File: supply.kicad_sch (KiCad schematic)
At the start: 62 parts, among them Q1 BSS138PW,115, Q6 BSS138PW,115, U21 TPS62A06DRLR, U22 TPS62A06DRLR, U40 SIC431AED-T1-GE3

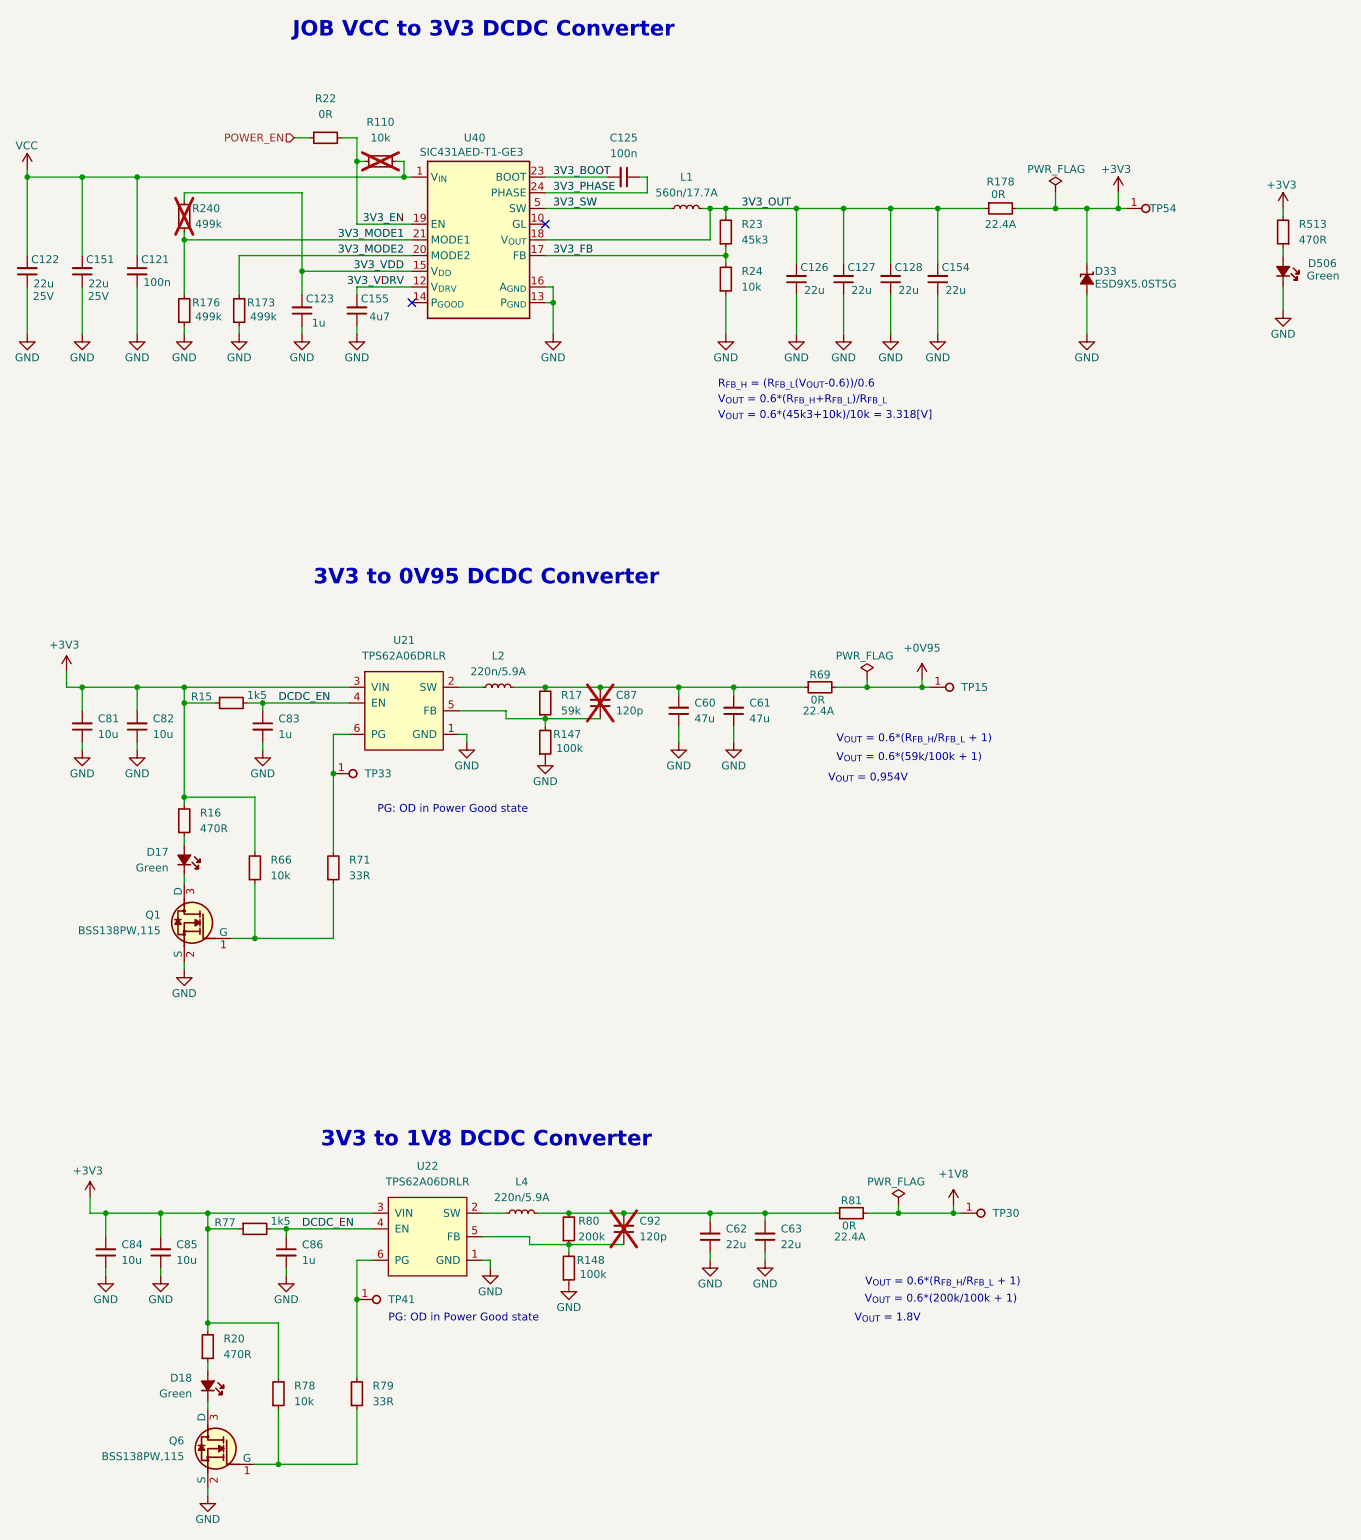
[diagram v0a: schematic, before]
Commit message: [#100765] Reset designators
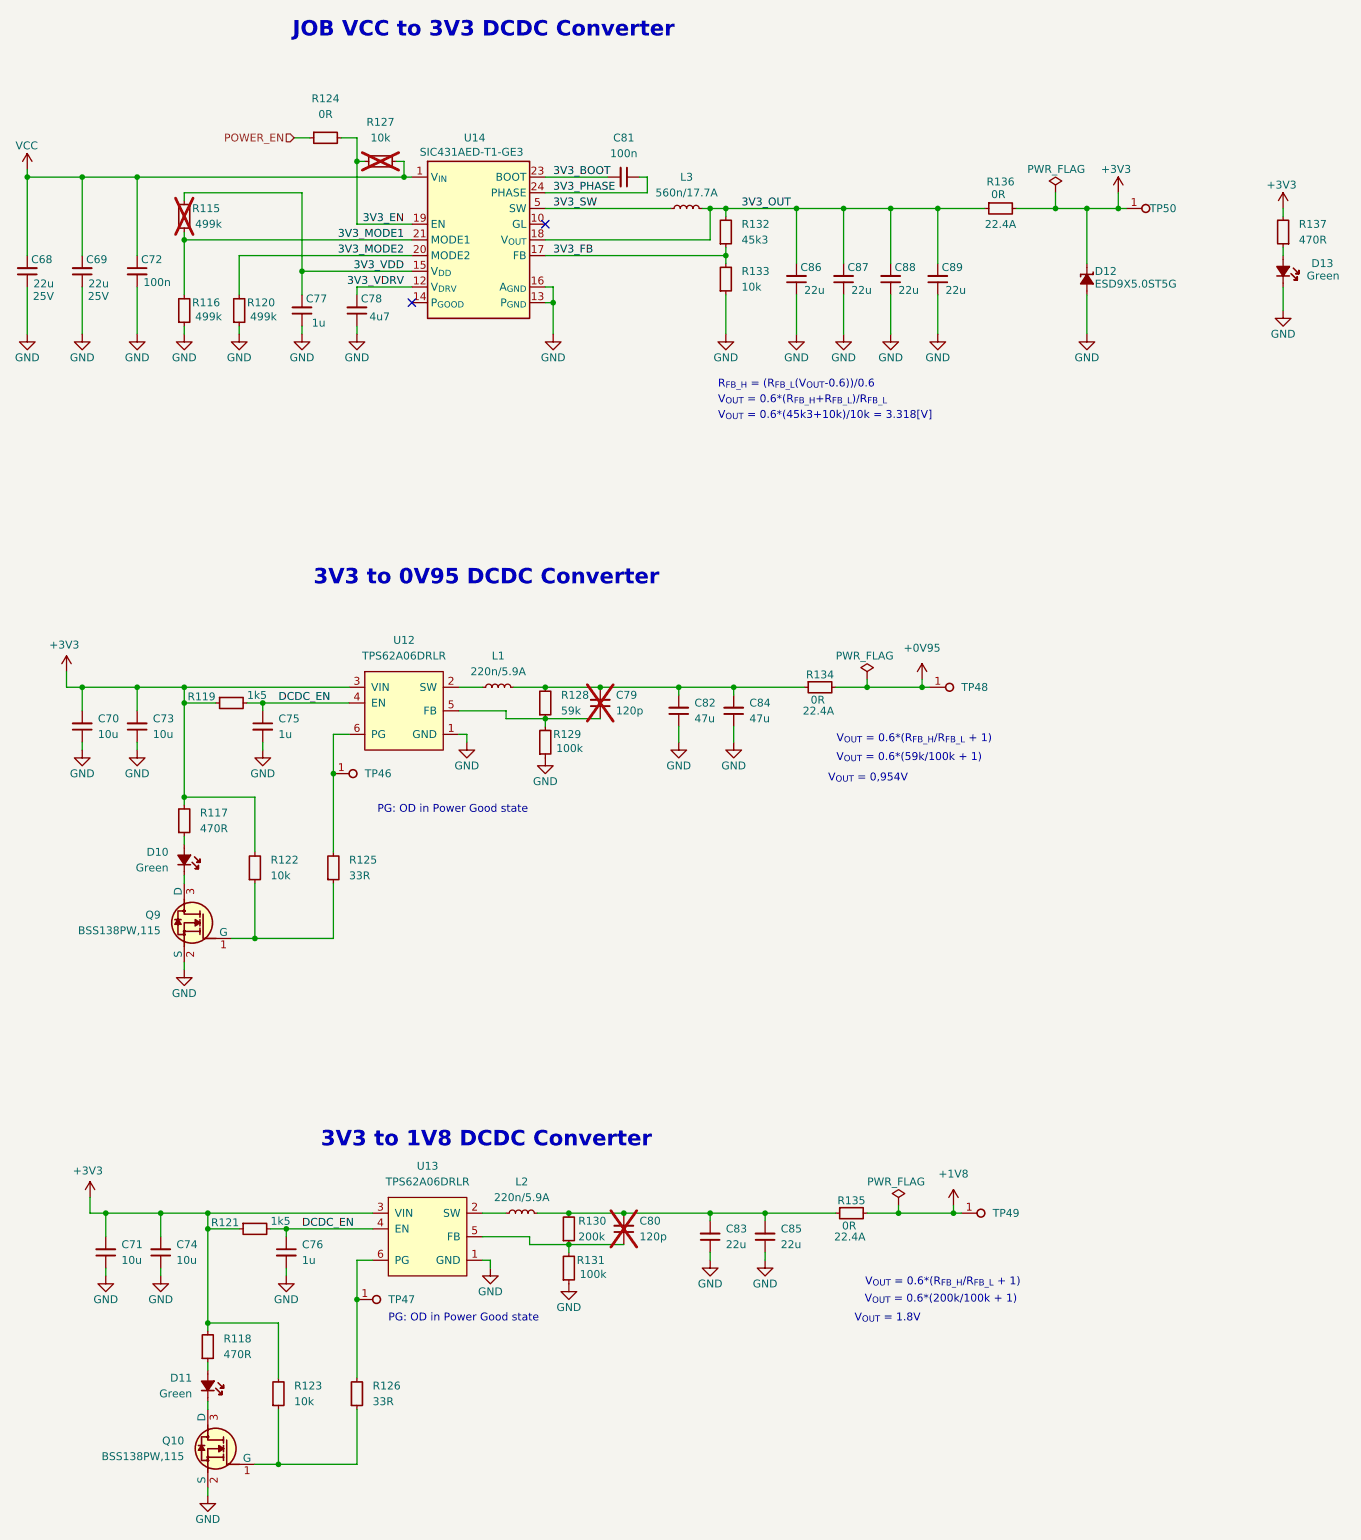
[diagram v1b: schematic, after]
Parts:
- renumbered C122 to C68, C151 to C69, C81 to C70, C84 to C71, C121 to C72, C82 to C73, C85 to C74, C83 to C75, C86 to C76, C123 to C77, C155 to C78, C87 to C79, C92 to C80, C125 to C81, C60 to C82, C62 to C83, C61 to C84, C63 to C85, C126 to C86, C127 to C87, C128 to C88, C154 to C89, D17 to D10, D18 to D11, D33 to D12, D506 to D13, L2 to L1, L4 to L2, L1 to L3, Q6 to Q10, Q1 to Q9, R240 to R115, R176 to R116, R16 to R117, R20 to R118, R15 to R119, R173 to R120, R77 to R121, R66 to R122, R78 to R123, R22 to R124, R71 to R125, R79 to R126, R110 to R127, R17 to R128, R147 to R129, R80 to R130, R148 to R131, R23 to R132, R24 to R133, R69 to R134, R81 to R135, R178 to R136, R513 to R137, TP33 to TP46, TP41 to TP47, TP15 to TP48, TP30 to TP49, TP54 to TP50, U21 to U12, U22 to U13, U40 to U14

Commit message: [#100765] Prettify schematic
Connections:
- net DCDC_EN: no longer names the net of C76.1, R121.2, U13.4 (EN)
- net DCDC_EN: no longer C75.1, R119.2, U12.4 (EN)
- new net: C75.1, R119.2, U12.4 (EN)
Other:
- note removed: "PG: OD in Power Good state"
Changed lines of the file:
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@@
 		)
 	)
-	(text "PG: OD in Power Good state"
-		(exclude_from_sim no)
-		(at 185.674 156.972 0)
-		(effects
-			(font
-				(size 1.27 1.27)
-			)
-		)
-	)
 	(text "3V3 to 0V95 DCDC Converter"
 		(exclude_from_sim no)
@@
 		)
 	)
-	(text "PG: OD in Power Good state"
-		(exclude_from_sim no)
-		(at 187.452 239.268 0)
-		(effects
-			(font
-				(size 1.27 1.27)
-			)
-		)
-	)
 	(text "V_{OUT} = 0,954V"
 		(exclude_from_sim no)
@@
 		)
 	)
-	(label "DCDC_EN"
-		(at 157.48 139.7 0)
-		(effects
-			(font
-				(size 1.27 1.27)
-				(thickness 0.1588)
-			)
-			(justify left bottom)
-		)
-	)
 	(label "3V3_MODE2"
 		(at 177.8 67.31 180)
@@
 		)
 	)
-	(label "DCDC_EN"
-		(at 161.29 224.79 0)
-		(effects
-			(font
-				(size 1.27 1.27)
-				(thickness 0.1588)
-			)
-			(justify left bottom)
-		)
-	)
